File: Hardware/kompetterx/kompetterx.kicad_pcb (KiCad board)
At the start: 4 copper layers, 147 x 87 mm, 96 parts, among them J1 OLED_01x04, J2 SPI2_01x05, J3 Programming, J4 +12V PWR, J5 USB_C_Receptacle_USB2.0, Q1 AO3401A, SW1 SW_SPDT, SW10 SW_Push, SW11 SW_Push, SW12 SW_Push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

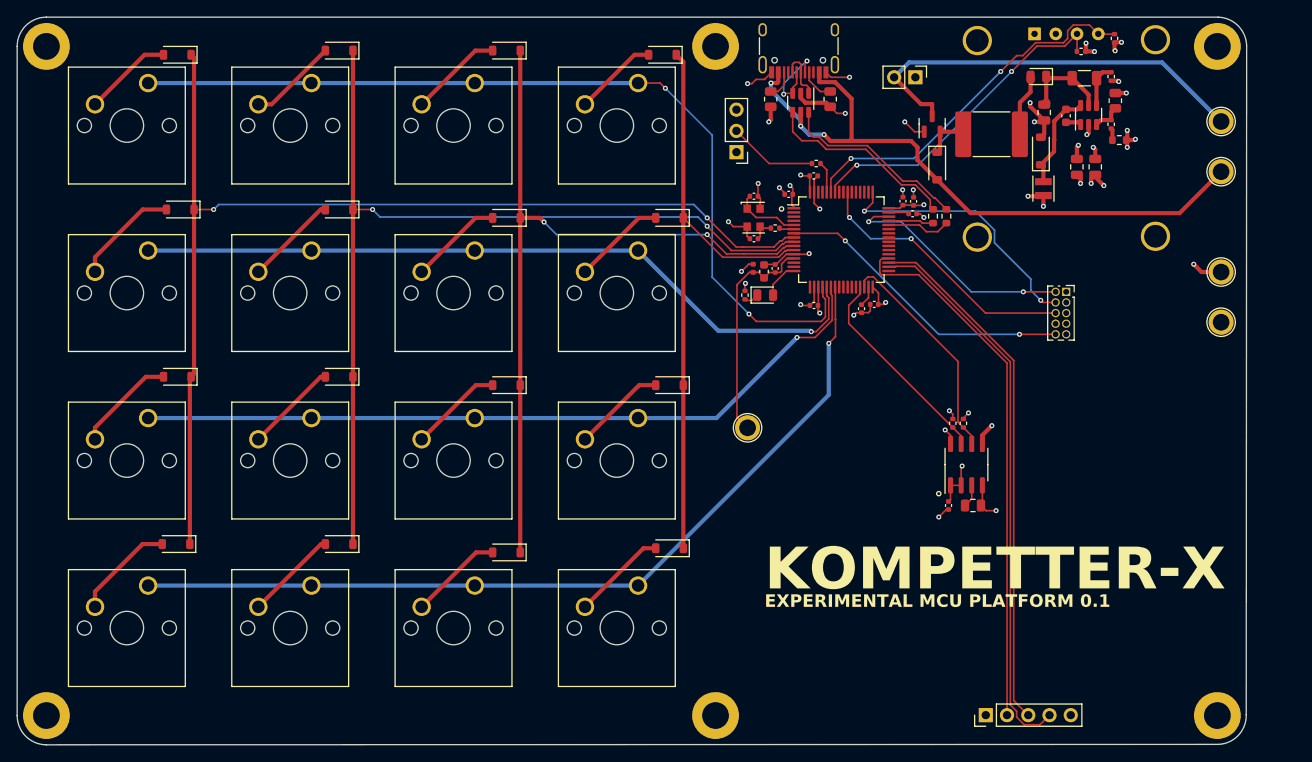
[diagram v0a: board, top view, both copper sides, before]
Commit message: Update USB-bug hardware + software
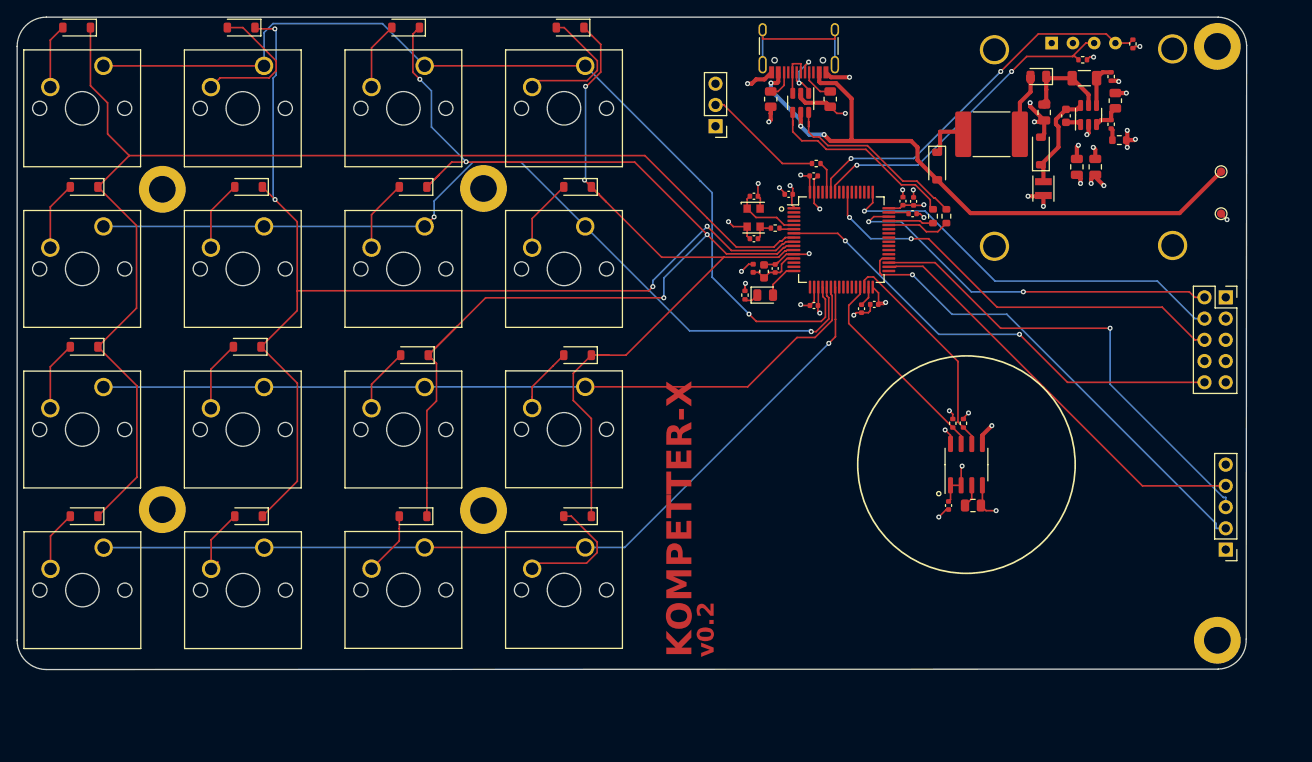
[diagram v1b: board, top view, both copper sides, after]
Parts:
- removed J4: +12V PWR, Connector_PinHeader_2.54mm:PinHeader_1x02_P2.54mm_Vertical
- removed Q1: AO3401A, Package_TO_SOT_SMD:SOT-23
- removed TP1, TP3, TP4: TestPoint, TestPoint:TestPoint_Plated_Hole_D2.0mm
- J3: footprint Connector_PinSocket_1.27mm:PinSocket_2x05_P1.27mm_Vertical -> Connector_PinSocket_2.54mm:PinSocket_2x05_P2.54mm_Vertical
- TP2, TP5: footprint TestPoint:TestPoint_Plated_Hole_D2.0mm -> TestPoint:TestPoint_Pad_D1.0mm
- moved H1 37.0 mm to (132.3, 95.5)
- moved J2 34.9 mm to (221.0, 100.2), turned to 180 degrees
- moved H4 32.5 mm to (132.3, 57.0)
- moved H2 28.2 mm to (93.9, 95.4)
- moved H3 22.0 mm to (93.9, 57.1)
- moved J3 19.1 mm to (221.0, 70.0)
- moved TP5 13.0 mm to (220.4, 60.0)
- moved D4 12.5 mm to (83.6, 37.7)
- moved D6 12.4 mm to (122.9, 37.7)
- moved D5 12.0 mm to (103.3, 37.7)
- moved D18 12.0 mm to (123.8, 96.2)
- moved D8 11.8 mm to (84.5, 56.8)
- moved D10 11.8 mm to (123.8, 56.8)
- moved D12 11.7 mm to (84.5, 75.9)
- moved D19 11.6 mm to (143.5, 96.2)
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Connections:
- J5 pad A6: USB_CONN_D- -> USB_CONN_D+
- J5 pad A7: USB_CONN_D+ -> USB_CONN_D-
- J5 pad B6: USB_CONN_D- -> USB_CONN_D+
- J5 pad B7: USB_CONN_D+ -> USB_CONN_D-
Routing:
- net +12V: track 50.0 -> 0.00 mm
- net KEY_COL_3: track 94.9 -> 137.6 mm, vias 2 -> 4
- net KEY_COL_4: track 74.9 -> 96.7 mm, vias 0 -> 2
- net KEY_COL_1: track 133.4 -> 154.0 mm, vias 2 -> 0
- net +3.3VA: track 26.8 -> 6.61 mm
- net NRST: track 36.3 -> 56.5 mm
- net KEY_COL_2: track 114.2 -> 134.2 mm, vias 2 -> 4
- net unconnected-(J5-SHIELD-PadS1): track 0.00 -> 19.2 mm
- net SWO: track 32.5 -> 51.6 mm
- net SWDIO: track 28.5 -> 46.6 mm
- net SWCLK: track 31.7 -> 48.7 mm, vias 2 -> 1
- net SPI2_SCK: track 66.9 -> 51.2 mm
- net KEY_ROW_2: track 89.9 -> 104.0 mm, vias 1 -> 2
- net KEY_ROW_1: track 106.7 -> 115.4 mm, vias 2 -> 1
- net SPI2_MOSI: track 64.4 -> 57.0 mm, vias 0 -> 1
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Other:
- board size 147 x 87 mm -> 147 x 78 mm
- board text added: "v0.2"
- board text removed: "EXPERIMENTAL MCU PLATFORM 0.1"
